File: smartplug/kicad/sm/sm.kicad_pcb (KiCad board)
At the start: 2 copper layers, 128.8 x 84.8 mm, 27 parts, among them J1 Screw_Terminal_01x02, J2 Screw_Terminal_01x02, J3 Screw_Terminal_01x02, J4 Screw_Terminal_01x03, J5 Screw_Terminal_01x02, J6 Screw_Terminal_01x02, J7 Screw_Terminal_01x03, J8 Screw_Terminal_01x02, J9 Conn_01x06_Male, U1 RELE QC3F-05VDC (10A 125-220 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, U2 ESP8266 ESP-12F, U3 Transformador100v-240v_5V_0.6A

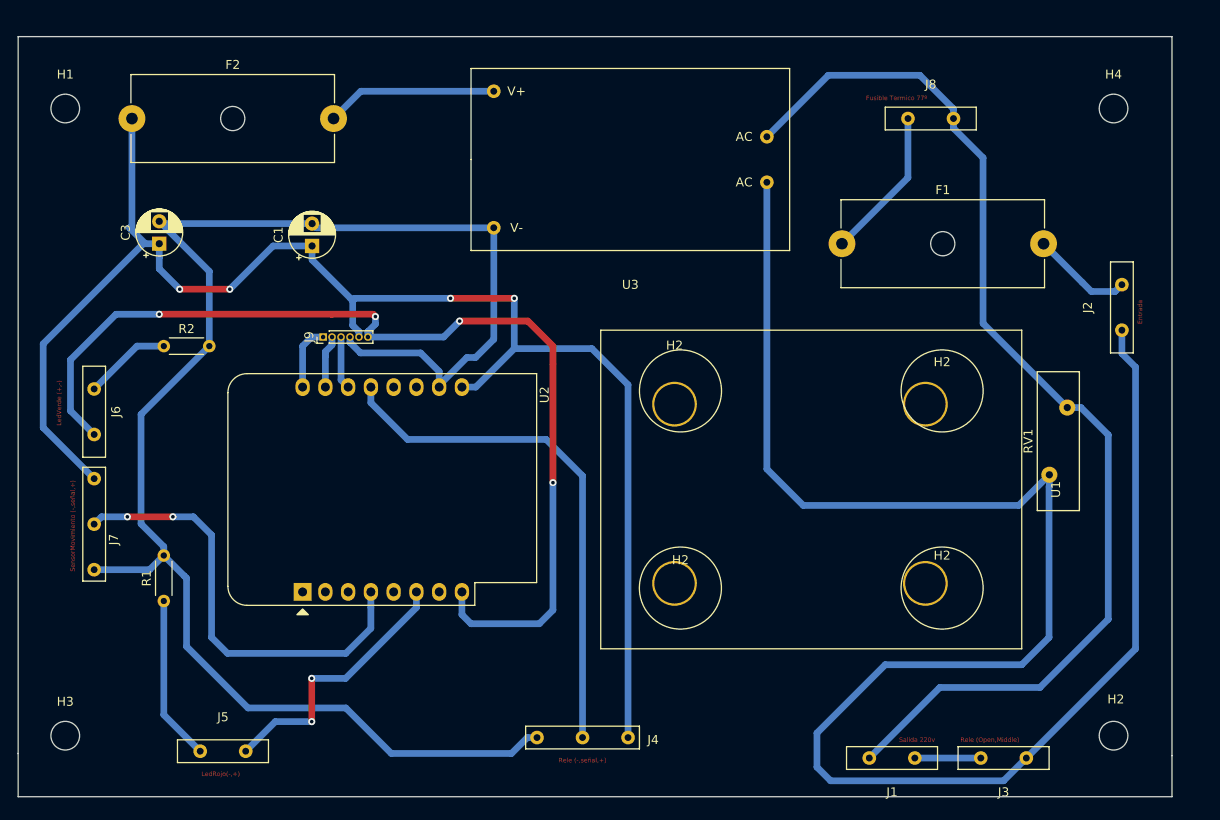
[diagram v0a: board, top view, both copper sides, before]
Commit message: Placa mas pequeña
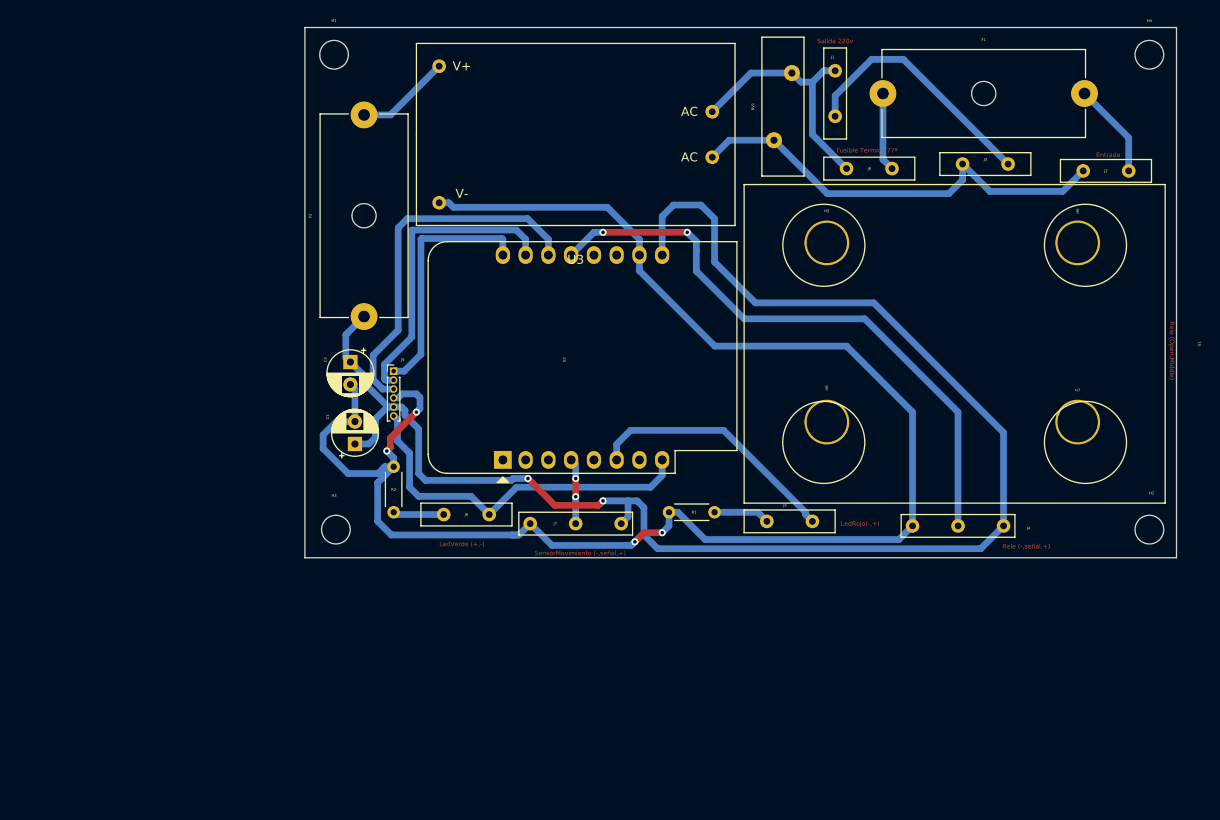
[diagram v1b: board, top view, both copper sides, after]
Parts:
- moved J1 74.4 mm to (185.9, 68.3), turned to 270 degrees
- moved J5 68.3 mm to (180.8, 116.1)
- moved J3 66.3 mm to (202.7, 76.2), turned to 180 degrees
- moved R1 62.3 mm to (172.5, 115.1), turned to 180 degrees
- moved J7 53.7 mm to (157.0, 116.3), turned to 0 degrees
- moved RV1 48.4 mm to (181.1, 66.0)
- moved J4 48.1 mm to (199.6, 116.6)
- moved J6 43.1 mm to (144.8, 115.3), turned to 180 degrees
- moved H3 37.8 mm to (130.0, 117.0)
- moved F2 34.1 mm to (133.3, 93.2), turned to 90 degrees
- moved R2 31.7 mm to (136.7, 115.1), turned to 90 degrees
- moved H1 30.6 mm to (130.0, 64.0)
- moved U2 26.8 mm to (148.8, 109.2)
- moved C3 25.1 mm to (131.8, 98.3), turned to 270 degrees
- moved H8 25.0 mm to (185.0, 105.0)
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- renumbered H2 to H5, H2 to H6, H2 to H7, H2 to H8
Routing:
- net /Linea2: track 197.8 -> 49.3 mm
- net Net-(J1-Pad1): track 123.3 -> 27.7 mm
- net +3V3: track 114.1 -> 41.7 mm, vias 4 -> 0
- net Net-(J7-Pad2): track 49.5 -> 7.32 mm
- net Net-(J9-Pad3): track 5.92 -> 40.7 mm
- net Net-(J9-Pad2): track 5.90 -> 33.8 mm
- net Net-(J1-Pad2): track 7.37 -> 28.1 mm
- net Net-(J9-Pad1): track 7.28 -> 27.6 mm
- net Net-(J5-Pad2): track 18.4 -> 6.26 mm
- net Net-(J4-Pad2): track 58.0 -> 67.2 mm, vias 0 -> 2
- net Net-(F2-Pad2): track 19.1 -> 10.6 mm
- net Net-(F1-Pad1): track 17.0 -> 8.80 mm
- net Net-(J6-Pad2): track 9.75 -> 5.69 mm
- net GND: track 180.4 -> 182.6 mm, vias 0 -> 4
- net Net-(J5-Pad1): track 30.3 -> 28.6 mm, vias 2 -> 0
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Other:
- board size 128.8 x 84.8 mm -> 97.3 x 59.2 mm
